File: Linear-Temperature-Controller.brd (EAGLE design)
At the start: 203.2 x 34.3 mm, 70 parts, among them IC1 LM393D, IC3 AD5624R, IC4 AD5262, IC5 OP27, T1 MMBT3904, T2 MMBT3904

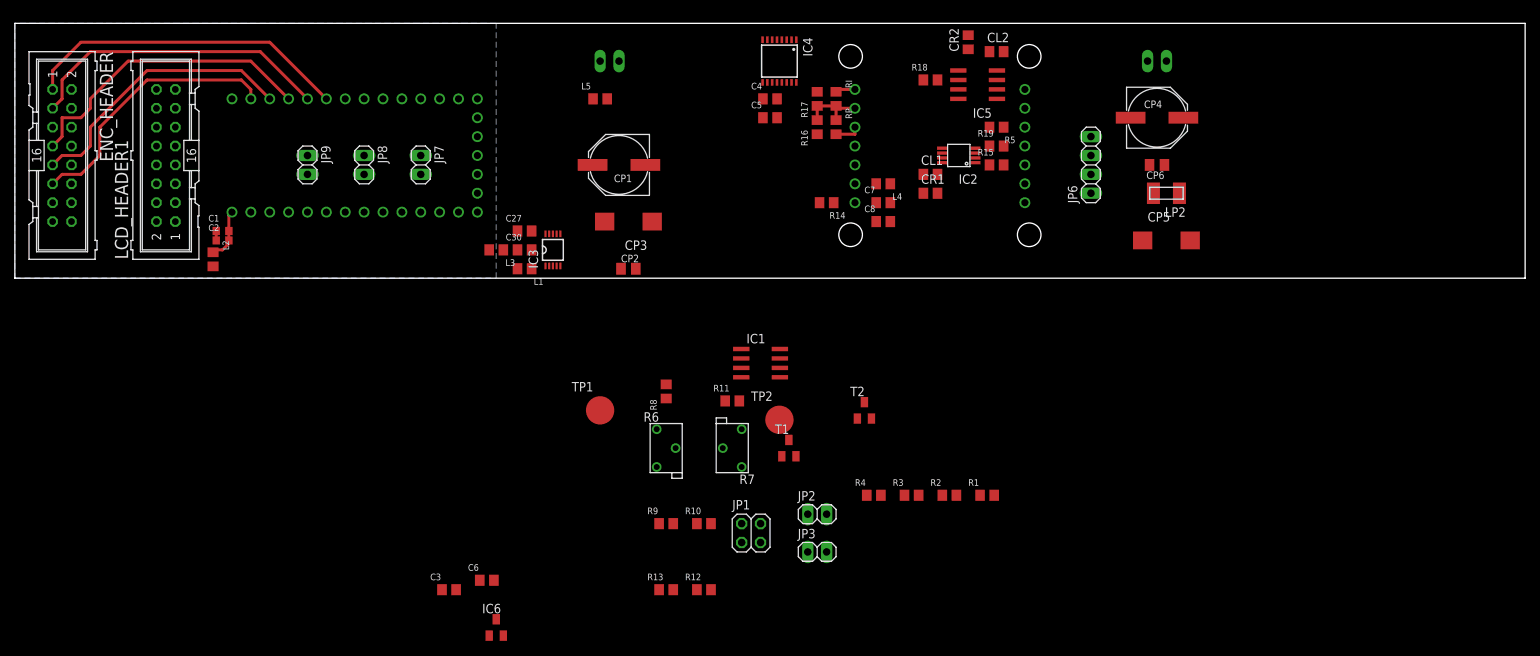
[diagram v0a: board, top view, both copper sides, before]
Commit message: Progress...
Added voltage divider to Teensy analog inputs, added a couple extra
teensy channels, layout progress
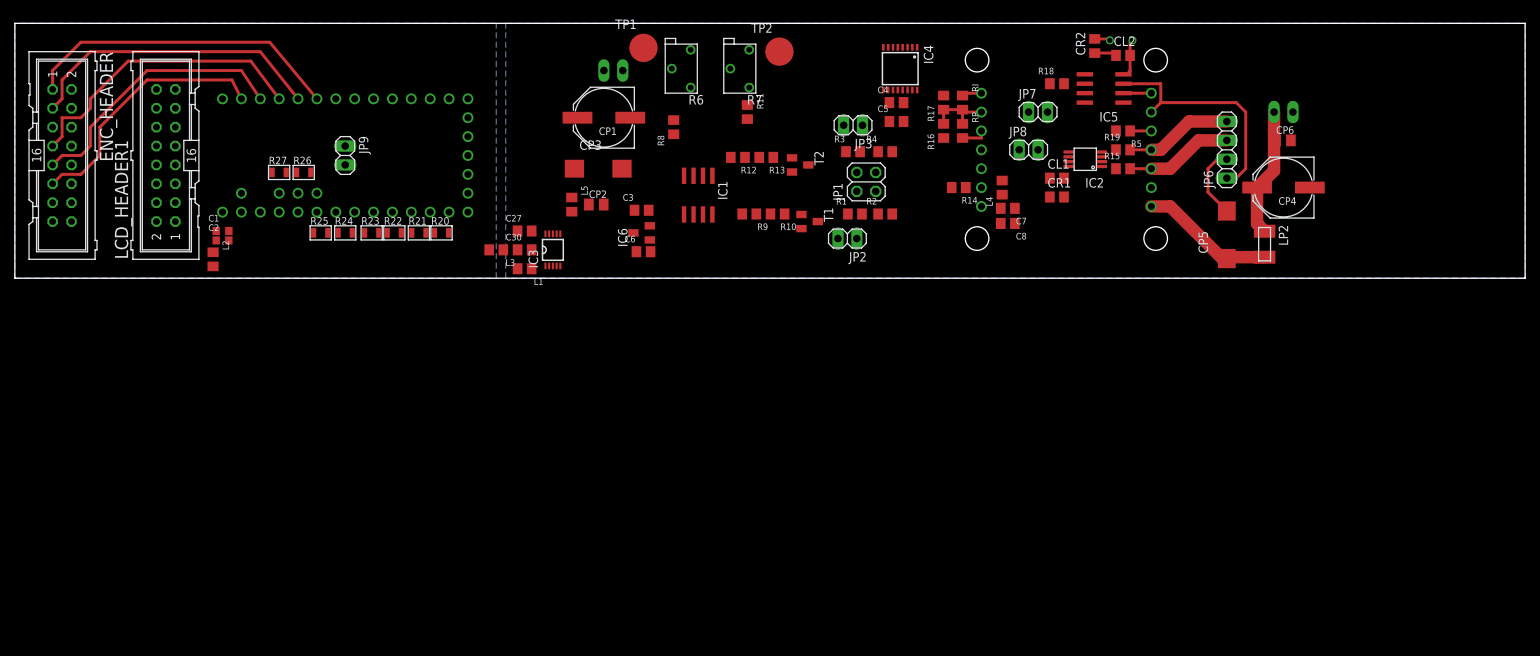
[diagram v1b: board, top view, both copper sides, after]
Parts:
- added R20, R21, R22, R23, R24, R25, R26, R27: 10k, jqi_passives:R_0805
- U$1: value TEENSY_3.1_BASIC -> TEENSY_3.1+4; device mcu-accessories:TEENSY_3.1_BASIC -> mcu-accessories:TEENSY_3.1+4
- moved JP8 89.4 mm to (136.4, 17.3), turned to 0 degrees
- moved JP7 83.4 mm to (137.7, 22.4), turned to 0 degrees
- moved R13 59.7 mm to (101.1, 16.3), turned to 180 degrees
- moved R12 58.3 mm to (97.3, 16.3), turned to 180 degrees
- moved JP3 57.6 mm to (112.8, 20.6), turned to 180 degrees
- moved C3 57.3 mm to (84.3, 9.14)
- moved IC6 56.6 mm to (84.3, 6.10), turned to 90 degrees
- moved R6 51.1 mm to (89.7, 28.2), turned to 180 degrees
- moved R7 51.1 mm to (97.5, 28.2)
- moved JP1 49.7 mm to (114.6, 13.0), turned to 90 degrees
- moved TP2 49.5 mm to (102.9, 30.5)
- moved TP1 49.1 mm to (84.6, 31.0)
- moved C6 49.0 mm to (84.6, 3.56)
- moved R3 46.9 mm to (112.8, 17.0)
- moved R4 46.3 mm to (117.1, 17.0)
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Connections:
- net N$21 renamed OUTB
- net N$22 renamed OUTA
- new net GND: IC4.12
- new net MOSI_B: IC4.8, U$1.23/A9
- new net SCK_B: IC4.7, U$1.22/A8
- new net VMON1_B: R26.P$1, R27.P$2, U$1.A10
- new net VMON2_B: R24.P$1, R25.P$2, U$1.19/A5
- new net VMON3_B: R22.P$1, R23.P$2, U$1.17/A3
- new net VMON4_B: R20.P$1, R21.P$2, U$1.15/A1
- new net VUSB: U$1.VUSB
- net 2.5V: now also U$1.AREF
- net ACT_T1: now also U$1.A11; no longer U$1.22/A8
- net AGND: now also C7.1, C8.1, R21.P$1, R23.P$1, R25.P$1, R27.P$1; no longer IC4.12
- net DGND: no longer C7.1, C8.1
- net MOSI: no longer IC4.8
- net N$99: now also U$1.21/A7; no longer U$1.23/A9
- net SCK: no longer IC4.7
- net VMON1: now also R26.P$2; no longer U$1.21/A7
- net VMON2: now also R24.P$2; no longer U$1.19/A5
- net VMON3: now also R22.P$2; no longer U$1.17/A3
- net VMON4: now also R20.P$2; no longer U$1.15/A1
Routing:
- net N$13: track 0.00 -> 32.0 mm
- net VSS: track 0.00 -> 18.2 mm
- net V+: track 0.00 -> 17.4 mm
- net AGND: track 0.00 -> 17.3 mm, vias 0 -> 2
- net OUTB: track 0.00 -> 14.6 mm
- net OUTA: track 0.00 -> 14.6 mm
- net N$25: track 7.01 -> 0.00 mm
- net N$23: track 0.00 -> 3.75 mm
- net VDD: track 0.00 -> 2.99 mm
- net N$5: track 0.00 -> 2.86 mm
- net ENC_SW1: track 36.5 -> 35.0 mm
- net DGND: track 1.27 -> 0.00 mm
- net ENC_A2: track 44.1 -> 43.2 mm
- net ENC_B2: track 41.6 -> 40.7 mm
- net ENC_A1: track 40.8 -> 40.0 mm
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- added copper zone on layer 16, net AGND
